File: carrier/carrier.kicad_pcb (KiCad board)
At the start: 4 copper layers, 14 x 12 mm, 2 parts, among them J1 DF40GB-30DP-0.4V(51), U1 TC58NVG1S3HBAI6

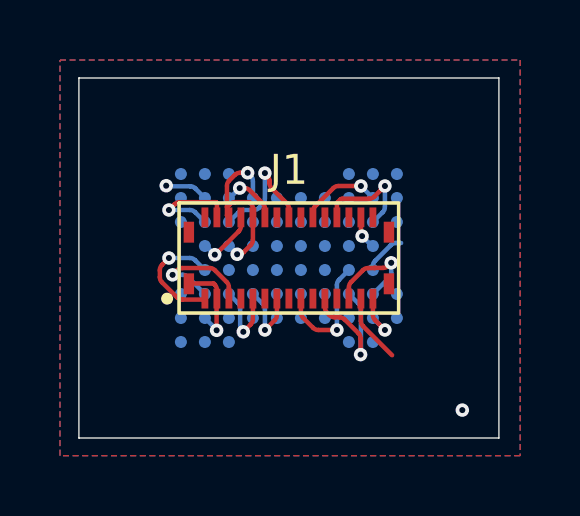
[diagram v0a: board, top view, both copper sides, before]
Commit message: Shrink carrier to 9.25 x 7.45 mm and add a GND stitching ring
Dropped local decoupling from the carrier after working the numbers
rather than assuming. Worst case is 8 I/O switching into 30 pF with
5 ns edges - 158 mA peak through 5.45 nH of loop - which is 173 mV,
5.2% of a 3.3 V rail against a 660 mV budget to VIH. At the 20-50 ns
edges a programmer actually produces it is 2-11 mV. The datasheet
specifies no bypass cap, DC is 30 mA max split over two DF40 contacts
rated 0.5 A each, and program/erase draw that over milliseconds with no
di/dt at all. The largest single inductance term is the carrier's own
J1-to-ball trace, which a local cap only partly shortens.

Decoupling therefore belongs on board B. Requirement recorded: 100 nF
within ~2 mm of the receptacle's VCC pins. Board B is 63 x 20 mm and
nearly empty, so it costs nothing there.

That frees the outline. 14 x 12 -> 9.25 x 7.45 mm, 168 -> 68.9 mm2, 59%
smaller. No rerouting was needed: all copper already sat inside
8.27 x 6.51 mm. Margins are >=0.32 mm to the package body and >=0.36 mm
to copper. JLCPCB's floor is 3 x 3 mm for FR4 at >=0.6 mm thickness, so
there is a lot of headroom left.

Added 15 GND stitching vias around the perimeter, one every ~2.2 mm,
inset 0.455 mm from the edge line. They only have to clear signal
copper, since every pour is GND. In1.Cu and In2.Cu are 52.1 mm2 each of
68.9, so 76% ground coverage.

DRC 0 violations, 0 unconnected.

Co-Authored-By: Claude Opus 5 <noreply@anthropic.com>
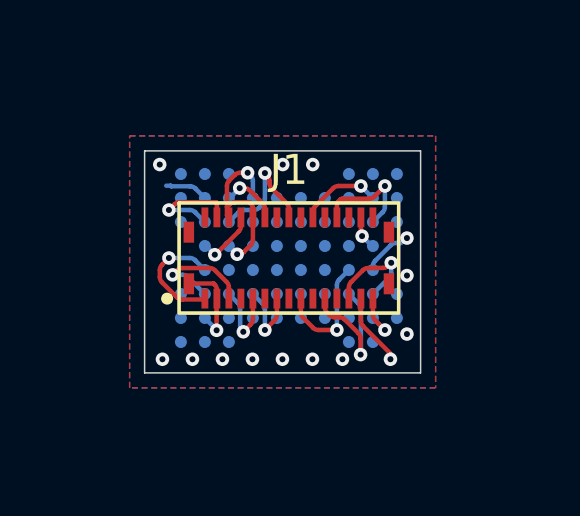
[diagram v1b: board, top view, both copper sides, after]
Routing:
- net GND: vias 3 -> 15
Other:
- board size 14 x 12 mm -> 9.2 x 7.4 mm

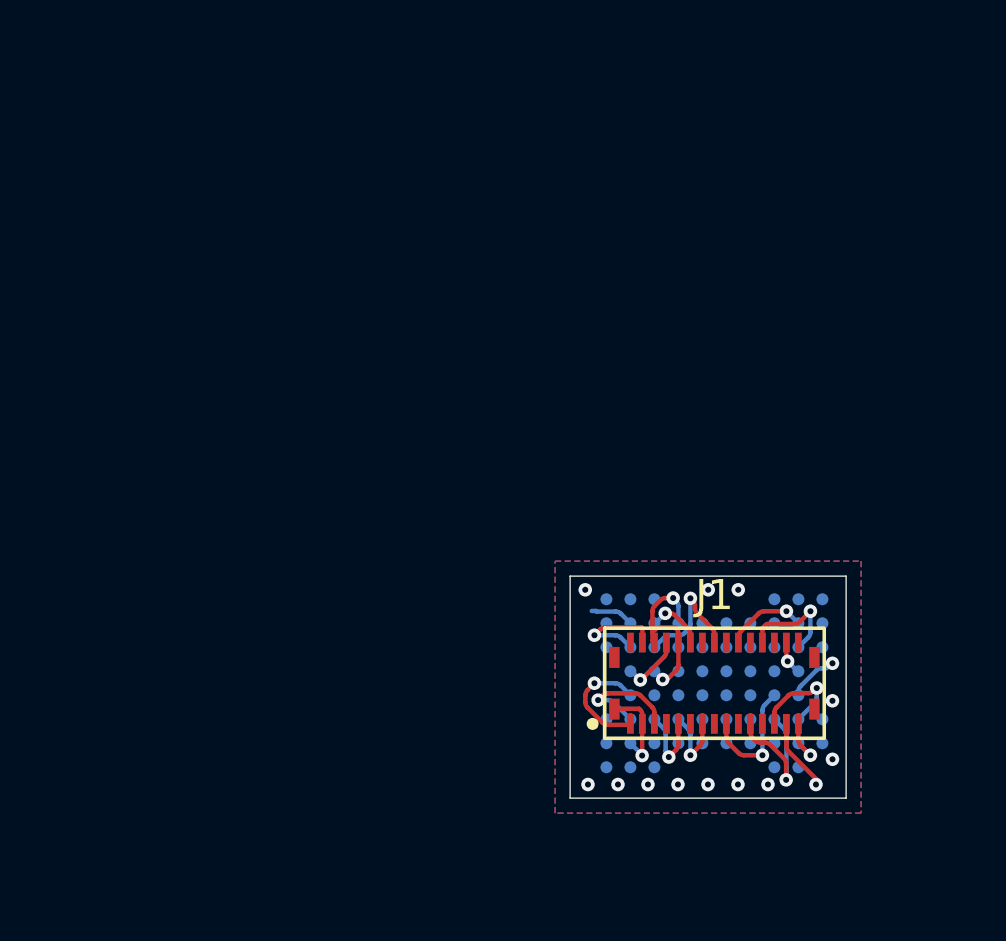
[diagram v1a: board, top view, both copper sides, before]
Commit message: Regenerate the panel against Alex's silkscreen edits
Carrier picked up two knockout F.SilkS texts, "REV A" and "VFBGA67",
plus a simplification of the footprint outlines, and the whole board was
translated. Copper is byte-for-byte the same set of 308 objects and the
outline is still 9.25 x 7.45 mm, so nothing electrical moved.

Panel rebuilt with the same recipe: 52.9 x 45.7 mm, 16 up, mouse bites
at -0.3 mm offset, 64 co-located drills deduped, fp-lib-table repointed
at ../carrier/lib. Both texts propagate to all 16 boards.

The silk simplification also cleared the 32 silk_over_copper warnings
the previous panel carried. Panel DRC is now 16 lib_footprint_mismatch
notes and nothing else - one per U1, expected, since the board copy of
the BGA footprint now differs from the library after the silk edit.

Carrier DRC: 0 violations, 0 unconnected.

Co-Authored-By: Claude Opus 5 <noreply@anthropic.com>
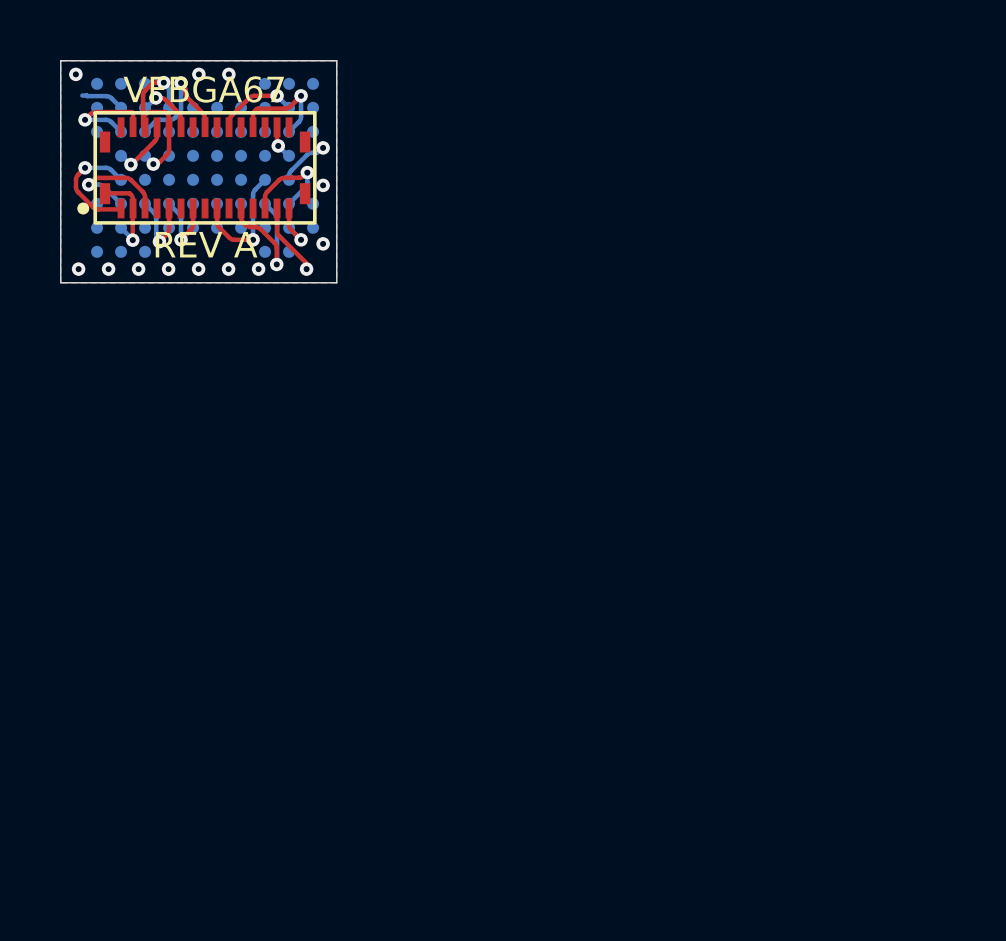
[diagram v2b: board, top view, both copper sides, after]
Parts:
- moved J1 24.2 mm to (168.5, 85.6)
- moved U1 24.2 mm to (168.5, 85.6)
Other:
- board text added: "REV A"
- board text added: "VFBGA67"
